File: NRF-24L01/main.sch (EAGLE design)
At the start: 17 parts

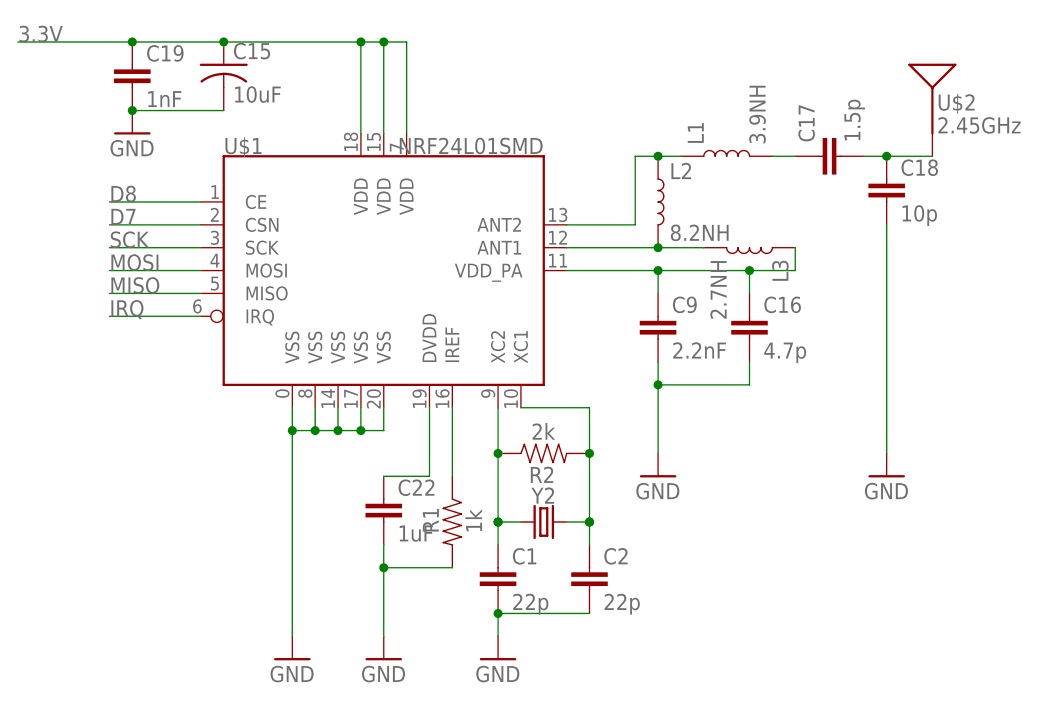
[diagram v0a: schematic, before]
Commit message: add license
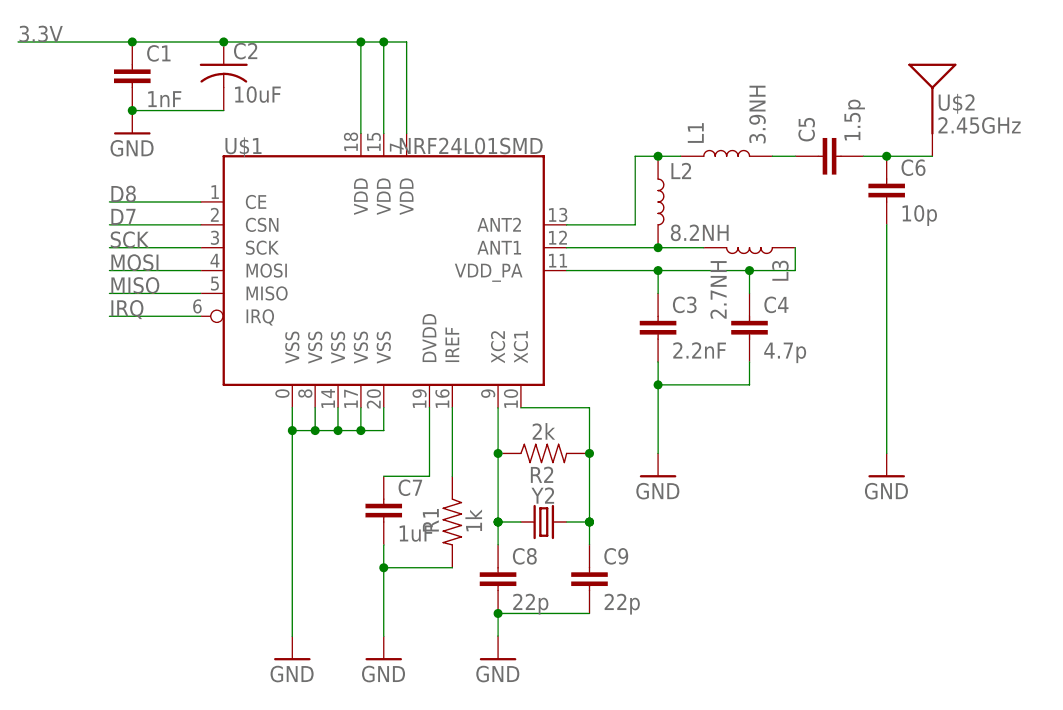
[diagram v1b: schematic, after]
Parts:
- removed C15: 10uF, adafruit:C-USC1206
- removed C19: 1nF, SparkFun-Passives:CAP0805
- added C3: 2.2nF, SparkFun-Passives:CAP0805
- added C8: 22p, SparkFun-Passives:CAP0805
- C1: value 22p -> 1nF
- C2: value 22p -> 10uF; device SparkFun-Passives:CAP0805 -> adafruit:C-USC1206
- C9: value 2.2nF -> 22p
- renumbered C16 to C4, C17 to C5, C18 to C6, C22 to C7
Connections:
- net 3.3V: now also C1.1, C2.1; no longer C15.1, C19.1
- net GND: now also C3.2, C8.2; no longer C15.2, C19.2
- net N$16: now also C3.1; no longer C9.1
- net N$20: now also C8.1; no longer C1.1
- net N$21: now also C9.1; no longer C2.1
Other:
- moved on the sheet: C1, C2, C9
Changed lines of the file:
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@@
 <part name="U$1" library="SparkFun-RF" library_urn="urn:adsk.eagle:library:531" deviceset="NRF24L01" device="SMD" package3d_urn="urn:adsk.eagle:package:39549/1"/>
 <part name="GND1" library="SparkFun-Aesthetics" deviceset="GND" device=""/>
-<part name="C15" library="adafruit" deviceset="C-US" device="C1206" value="10uF"/>
+<part name="C2" library="adafruit" deviceset="C-US" device="C1206" value="10uF"/>
 <part name="GND2" library="SparkFun-Aesthetics" deviceset="GND" device=""/>
 <part name="GND3" library="SparkFun-Aesthetics" deviceset="GND" device=""/>
@@
 <part name="L2" library="SparkFun-Coils" library_urn="urn:adsk.eagle:library:512" deviceset="INDUCTOR" device="-0402-3.9NH" package3d_urn="urn:adsk.eagle:package:37575/1" value="8.2NH"/>
 <part name="L3" library="SparkFun-Coils" library_urn="urn:adsk.eagle:library:512" deviceset="INDUCTOR" device="-0402-3.9NH" package3d_urn="urn:adsk.eagle:package:37575/1" value="2.7NH"/>
-<part name="C17" library="SparkFun-Passives" deviceset="CAP" device="0805" value="1.5p"/>
-<part name="C18" library="SparkFun-Passives" deviceset="CAP" device="0805" value="10p"/>
+<part name="C5" library="SparkFun-Passives" deviceset="CAP" device="0805" value="1.5p"/>
+<part name="C6" library="SparkFun-Passives" deviceset="CAP" device="0805" value="10p"/>
 <part name="GND9" library="SparkFun-Aesthetics" deviceset="GND" device=""/>
-<part name="C9" library="SparkFun-Passives" deviceset="CAP" device="0805" value="2.2nF"/>
-<part name="C16" library="SparkFun-Passives" deviceset="CAP" device="0805" value="4.7p"/>
-<part name="C22" library="SparkFun-Passives" deviceset="CAP" device="0805" value="1uF"/>
-<part name="C19" library="SparkFun-Passives" deviceset="CAP" device="0805" value="1nF"/>
+<part name="C3" library="SparkFun-Passives" deviceset="CAP" device="0805" value="2.2nF"/>
+<part name="C4" library="SparkFun-Passives" deviceset="CAP" device="0805" value="4.7p"/>
+<part name="C7" library="SparkFun-Passives" deviceset="CAP" device="0805" value="1uF"/>
+<part name="C1" library="SparkFun-Passives" deviceset="CAP" device="0805" value="1nF"/>
 <part name="U$2" library="SparkFun-RF" library_urn="urn:adsk.eagle:library:531" deviceset="ANTENNA" device="2.4GHZ-6.5X2.2MM" package3d_urn="urn:adsk.eagle:package:39539/1" value="2.45GHz"/>
 <part name="R2" library="SparkFun-Resistors" deviceset="RESISTOR" device="0805-RES" value="2k"/>
 <part name="Y2" library="SparkFun-Clocks" library_urn="urn:adsk.eagle:library:511" deviceset="CRYSTAL" device="SMD-5X3.2-4PAD" package3d_urn="urn:adsk.eagle:package:37518/1"/>
-<part name="C1" library="SparkFun-Passives" deviceset="CAP" device="0805" value="22p"/>
-<part name="C2" library="SparkFun-Passives" deviceset="CAP" device="0805" value="22p"/>
+<part name="C8" library="SparkFun-Passives" deviceset="CAP" device="0805" value="22p"/>
+<part name="C9" library="SparkFun-Passives" deviceset="CAP" device="0805" value="22p"/>
 <part name="GND10" library="SparkFun-Aesthetics" deviceset="GND" device=""/>
 </parts>
@@
 <attribute name="VALUE" x="12.7" y="66.04" size="1.778" layer="96"/>
 </instance>
-<instance part="C15" gate="G$1" x="25.4" y="76.2" smashed="yes">
+<instance part="C2" gate="G$1" x="25.4" y="76.2" smashed="yes">
 <attribute name="NAME" x="26.416" y="76.835" size="1.778" layer="95"/>
 <attribute name="VALUE" x="26.416" y="72.009" size="1.778" layer="96"/>
@@
 <attribute name="VALUE" x="81.28" y="54.61" size="1.778" layer="96" font="vector" rot="R270" align="top-left"/>
 </instance>
-<instance part="C17" gate="G$1" x="93.98" y="66.04" smashed="yes" rot="R90">
+<instance part="C5" gate="G$1" x="93.98" y="66.04" smashed="yes" rot="R90">
 <attribute name="NAME" x="91.059" y="67.564" size="1.778" layer="95" rot="R90"/>
 <attribute name="VALUE" x="96.139" y="67.564" size="1.778" layer="96" rot="R90"/>
 </instance>
-<instance part="C18" gate="G$1" x="99.06" y="60.96" smashed="yes">
+<instance part="C6" gate="G$1" x="99.06" y="60.96" smashed="yes">
 <attribute name="NAME" x="100.584" y="63.881" size="1.778" layer="95"/>
 <attribute name="VALUE" x="100.584" y="58.801" size="1.778" layer="96"/>
@@
 <attribute name="VALUE" x="96.52" y="27.94" size="1.778" layer="96"/>
 </instance>
-<instance part="C9" gate="G$1" x="73.66" y="45.72" smashed="yes">
+<instance part="C3" gate="G$1" x="73.66" y="45.72" smashed="yes">
 <attribute name="NAME" x="75.184" y="48.641" size="1.778" layer="95"/>
 <attribute name="VALUE" x="75.184" y="43.561" size="1.778" layer="96"/>
 </instance>
-<instance part="C16" gate="G$1" x="83.82" y="45.72" smashed="yes">
+<instance part="C4" gate="G$1" x="83.82" y="45.72" smashed="yes">
 <attribute name="NAME" x="85.344" y="48.641" size="1.778" layer="95"/>
 <attribute name="VALUE" x="85.344" y="43.561" size="1.778" layer="96"/>
 </instance>
-<instance part="C22" gate="G$1" x="43.18" y="25.4" smashed="yes">
+<instance part="C7" gate="G$1" x="43.18" y="25.4" smashed="yes">
 <attribute name="NAME" x="44.704" y="28.321" size="1.778" layer="95"/>
 <attribute name="VALUE" x="44.704" y="23.241" size="1.778" layer="96"/>
 </instance>
-<instance part="C19" gate="G$1" x="15.24" y="73.66" smashed="yes">
+<instance part="C1" gate="G$1" x="15.24" y="73.66" smashed="yes">
 <attribute name="NAME" x="16.764" y="76.581" size="1.778" layer="95"/>
 <attribute name="VALUE" x="16.764" y="71.501" size="1.778" layer="96"/>
@@
 <attribute name="VALUE" x="60.96" y="23.368" size="1.778" layer="96" font="vector" align="top-center"/>
 </instance>
-<instance part="C1" gate="G$1" x="55.88" y="17.78" smashed="yes">
+<instance part="C8" gate="G$1" x="55.88" y="17.78" smashed="yes">
 <attribute name="NAME" x="57.404" y="20.701" size="1.778" layer="95"/>
 <attribute name="VALUE" x="57.404" y="15.621" size="1.778" layer="96"/>
 </instance>
-<instance part="C2" gate="G$1" x="66.04" y="17.78" smashed="yes">
+<instance part="C9" gate="G$1" x="66.04" y="17.78" smashed="yes">
 <attribute name="NAME" x="67.564" y="20.701" size="1.778" layer="95"/>
 <attribute name="VALUE" x="67.564" y="15.621" size="1.778" layer="96"/>
@@
 <wire x1="15.24" y1="71.12" x2="25.4" y2="71.12" width="0.1524" layer="91"/>
 <pinref part="GND1" gate="1" pin="GND"/>
-<pinref part="C15" gate="G$1" pin="2"/>
-<pinref part="C19" gate="G$1" pin="2"/>
+<pinref part="C2" gate="G$1" pin="2"/>
+<pinref part="C1" gate="G$1" pin="2"/>
 <junction x="15.24" y="71.12"/>
 </segment>
@@
 <wire x1="43.18" y1="22.86" x2="43.18" y2="20.32" width="0.1524" layer="91"/>
 <pinref part="GND2" gate="1" pin="GND"/>
-<pinref part="C22" gate="G$1" pin="2"/>
+<pinref part="C7" gate="G$1" pin="2"/>
 <pinref part="R1" gate="G$1" pin="2"/>
 <wire x1="43.18" y1="20.32" x2="43.18" y2="12.7" width="0.1524" layer="91"/>
@@
 <junction x="73.66" y="40.64"/>
 <pinref part="GND8" gate="1" pin="GND"/>
-<pinref part="C9" gate="G$1" pin="2"/>
-<pinref part="C16" gate="G$1" pin="2"/>
-</segment>
-<segment>
-<pinref part="C18" gate="G$1" pin="2"/>
+<pinref part="C3" gate="G$1" pin="2"/>
+<pinref part="C4" gate="G$1" pin="2"/>
+</segment>
+<segment>
+<pinref part="C6" gate="G$1" pin="2"/>
 <pinref part="GND9" gate="1" pin="GND"/>
 <wire x1="99.06" y1="58.42" x2="99.06" y2="33.02" width="0.1524" layer="91"/>
 </segment>
 <segment>
-<pinref part="C1" gate="G$1" pin="2"/>
-<pinref part="C2" gate="G$1" pin="2"/>
+<pinref part="C8" gate="G$1" pin="2"/>
+<pinref part="C9" gate="G$1" pin="2"/>
 <wire x1="55.88" y1="15.24" x2="66.04" y2="15.24" width="0.1524" layer="91"/>
 <pinref part="GND10" gate="1" pin="GND"/>
@@
 <wire x1="45.72" y1="78.74" x2="43.18" y2="78.74" width="0.1524" layer="91"/>
 <junction x="43.18" y="78.74"/>
-<pinref part="C15" gate="G$1" pin="1"/>
+<pinref part="C2" gate="G$1" pin="1"/>
 <junction x="25.4" y="78.74"/>
-<pinref part="C19" gate="G$1" pin="1"/>
+<pinref part="C1" gate="G$1" pin="1"/>
 <junction x="15.24" y="78.74"/>
 <label x="2.54" y="78.74" size="1.778" layer="95"/>
@@
 <pinref part="L3" gate="G$1" pin="1"/>
 <wire x1="88.9" y1="53.34" x2="88.9" y2="55.88" width="0.1524" layer="91"/>
-<pinref part="C9" gate="G$1" pin="1"/>
-<pinref part="C16" gate="G$1" pin="1"/>
+<pinref part="C3" gate="G$1" pin="1"/>
+<pinref part="C4" gate="G$1" pin="1"/>
 </segment>
 </net>
@@
 <wire x1="43.18" y1="30.48" x2="48.26" y2="30.48" width="0.1524" layer="91"/>
 <wire x1="48.26" y1="30.48" x2="48.26" y2="38.1" width="0.1524" layer="91"/>
-<pinref part="C22" gate="G$1" pin="1"/>
+<pinref part="C7" gate="G$1" pin="1"/>
 </segment>
 </net>
@@
 <net name="N$19" class="0">
 <segment>
-<pinref part="C18" gate="G$1" pin="1"/>
+<pinref part="C6" gate="G$1" pin="1"/>
 <wire x1="99.06" y1="66.04" x2="104.14" y2="66.04" width="0.1524" layer="91"/>
 <pinref part="U$2" gate="G$1" pin="SIGNAL"/>
-<pinref part="C17" gate="G$1" pin="2"/>
+<pinref part="C5" gate="G$1" pin="2"/>
 <wire x1="96.52" y1="66.04" x2="99.06" y2="66.04" width="0.1524" layer="91"/>
 <junction x="99.06" y="66.04"/>
@@
 <junction x="55.88" y="33.02"/>
 <wire x1="55.88" y1="33.02" x2="55.88" y2="25.4" width="0.1524" layer="91"/>
-<pinref part="C1" gate="G$1" pin="1"/>
+<pinref part="C8" gate="G$1" pin="1"/>
 <pinref part="Y2" gate="G$1" pin="1"/>
 <wire x1="55.88" y1="25.4" x2="55.88" y2="22.86" width="0.1524" layer="91"/>
@@
 <wire x1="66.04" y1="33.02" x2="66.04" y2="25.4" width="0.1524" layer="91"/>
 <junction x="66.04" y="33.02"/>
-<pinref part="C2" gate="G$1" pin="1"/>
+<pinref part="C9" gate="G$1" pin="1"/>
 <pinref part="Y2" gate="G$1" pin="2"/>
 <wire x1="66.04" y1="25.4" x2="66.04" y2="22.86" width="0.1524" layer="91"/>
@@
 <segment>
 <pinref part="L1" gate="G$1" pin="2"/>
-<pinref part="C17" gate="G$1" pin="1"/>
+<pinref part="C5" gate="G$1" pin="1"/>
 <wire x1="86.36" y1="66.04" x2="88.9" y2="66.04" width="0.1524" layer="91"/>
 </segment>
